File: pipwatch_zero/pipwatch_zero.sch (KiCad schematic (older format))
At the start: 0 parts

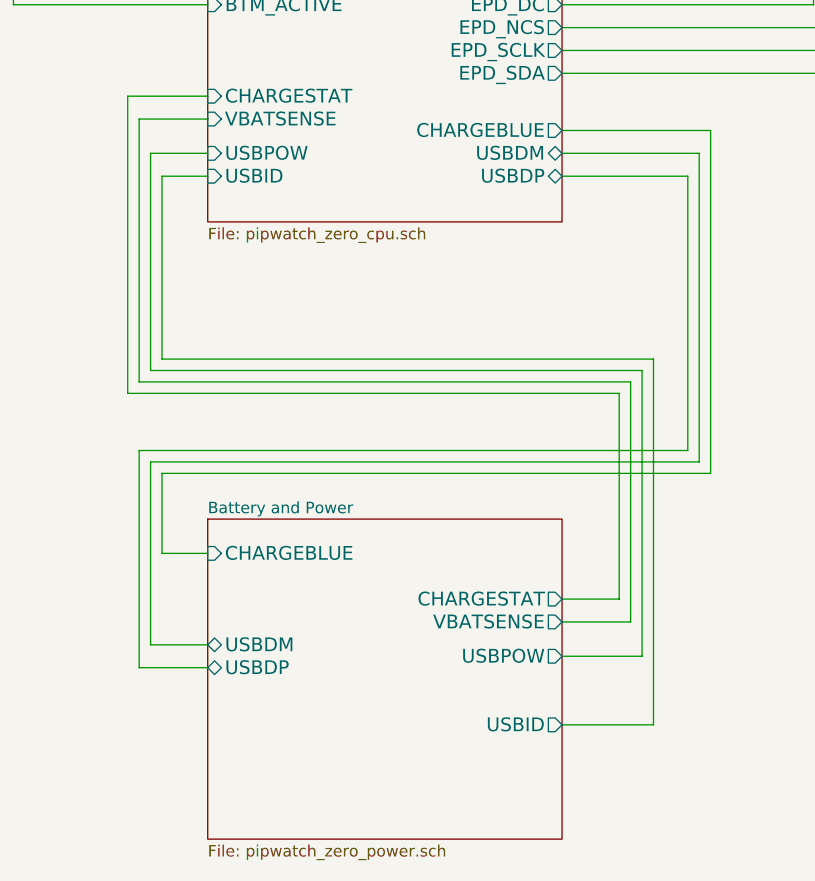
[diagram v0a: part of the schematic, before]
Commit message: pipwatch_zero layout complete
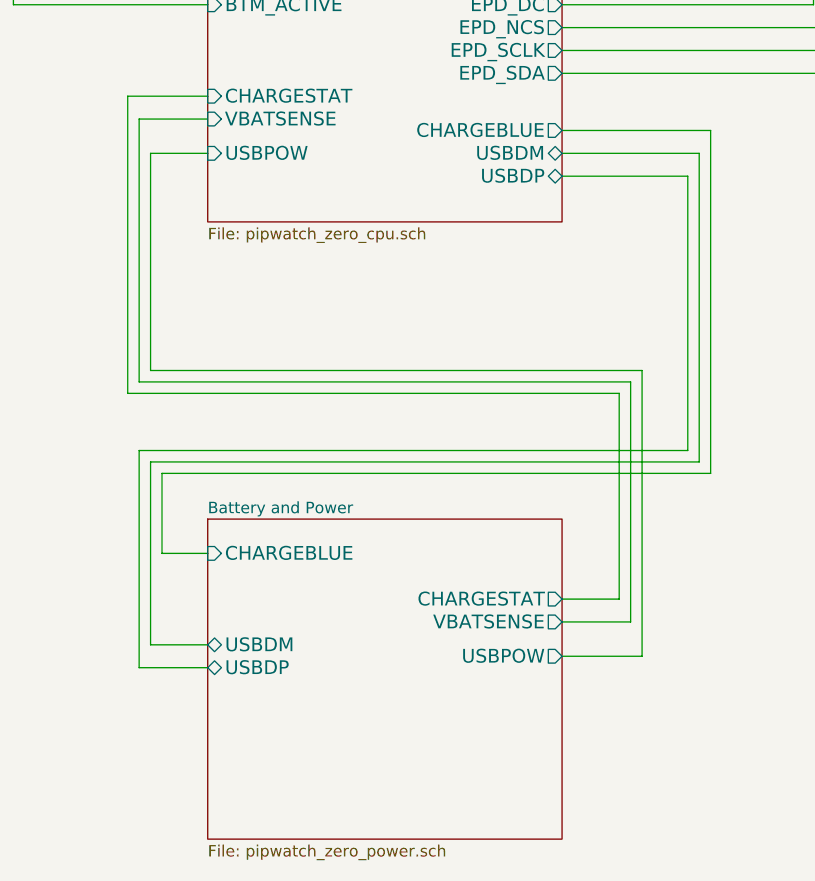
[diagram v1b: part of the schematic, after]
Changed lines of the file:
@@
 F5 "CHARGESTAT" O R 6700 5300 60
 F6 "CHARGEBLUE" I L 5150 5100 60
-F7 "USBID" O R 6700 5850 60
-F8 "USBDM" B L 5150 5500 60
+F7 "USBDM" B L 5150 5500 60
 $EndSheet
 $Sheet
@@
 F14 "USBDP" B R 6700 3450 60
 F15 "USBPOW" I L 5150 3350 60
-F16 "USBID" I L 5150 3450 60
-F17 "BTM_DTR" I L 5150 2500 60
-F18 "BTM_DSR" O R 6700 2300 60
-F19 "BTM_ACTIVE" I L 5150 2700 60
-F20 "CHARGESTAT" I L 5150 3100 60
-F21 "BTM_RESET" O R 6700 2400 60
-F22 "BTM_RI" I L 5150 2600 60
-F23 "CHARGEBLUE" O R 6700 3250 60
+F16 "BTM_DTR" I L 5150 2500 60
+F17 "BTM_DSR" O R 6700 2300 60
+F18 "BTM_ACTIVE" I L 5150 2700 60
+F19 "CHARGESTAT" I L 5150 3100 60
+F20 "BTM_RESET" O R 6700 2400 60
+F21 "BTM_RI" I L 5150 2600 60
+F22 "CHARGEBLUE" O R 6700 3250 60
 $EndSheet
 Wire Wire Line
@@
 Wire Wire Line
 	7050 4300 4900 4300
-Wire Wire Line
-	6700 5850 7100 5850
-Wire Wire Line
-	7100 5850 7100 4250
-Wire Wire Line
-	7100 4250 4950 4250
 $Sheet
 S 2200 2000 1500 1650
@@
 	4900 3350 4900 4300
 Wire Wire Line
-	4950 4250 4950 3450
-Wire Wire Line
-	4950 3450 5150 3450
-Wire Wire Line
 	6700 2600 7750 2600
